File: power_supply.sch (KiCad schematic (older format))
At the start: 68 parts, among them J1 USB-MICRO, J2 USB, Q1 SI4174DY, Q2 SI4463CDY, Q3 SW, U1 LM3914, U10 LT1494, U2 TPD2E001DRL, U3 MIC2185, U4 TPS2511, U5 MCP73833, U6 TPD2E001DRL, U7 BATT, U8 MAX9938T, U9 FDC6392S

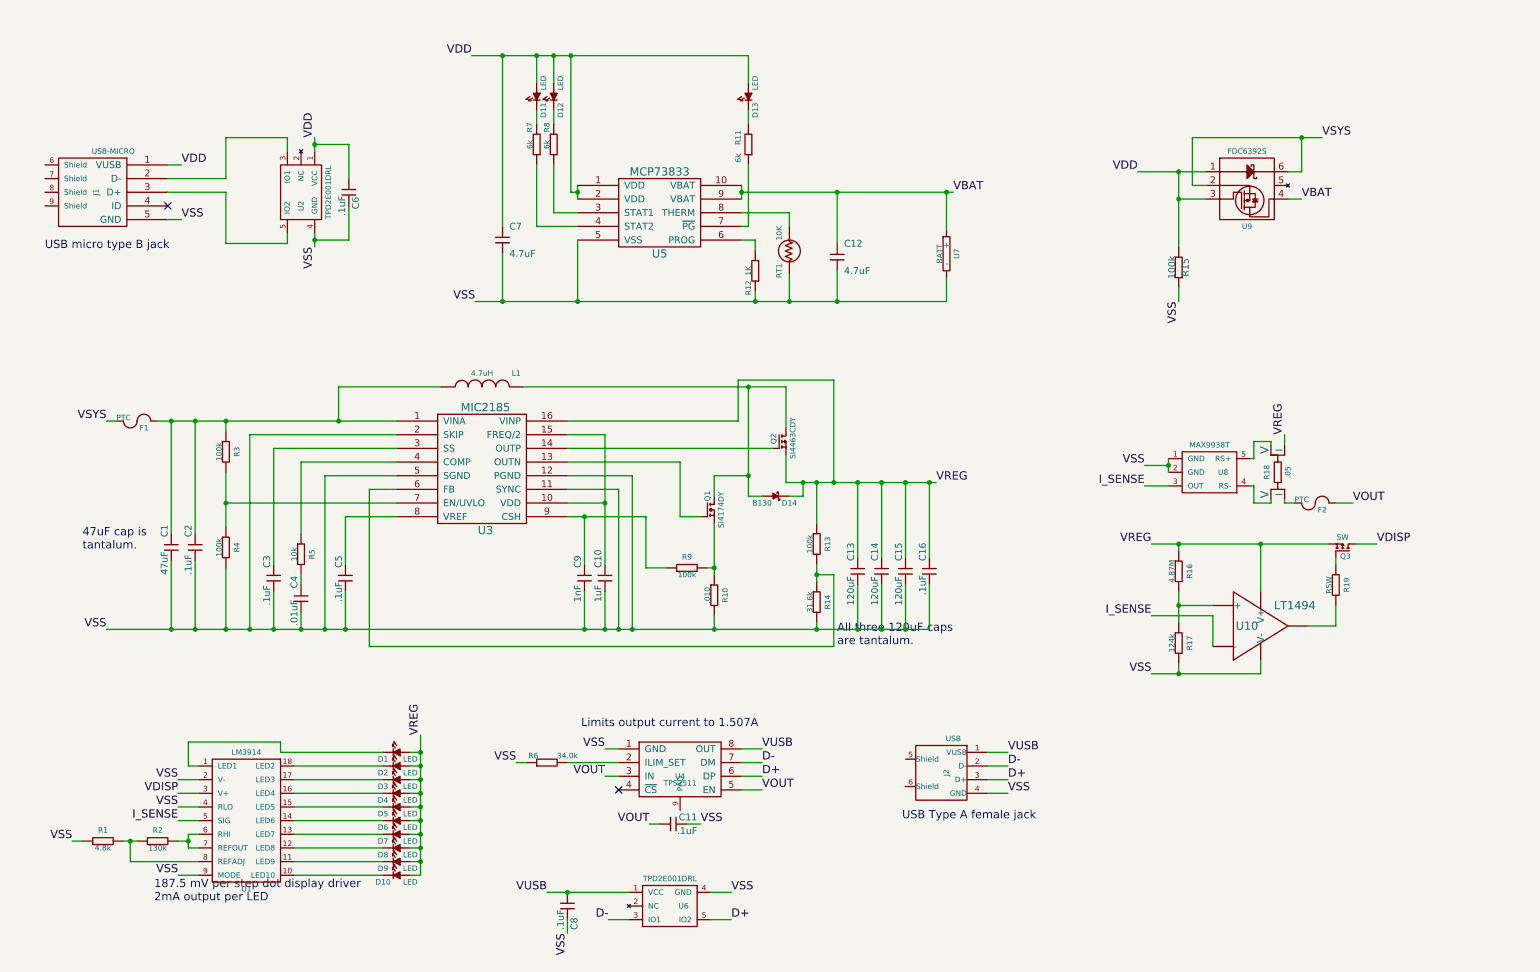
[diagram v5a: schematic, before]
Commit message: Updated comparator circuit to add histeresis.
Should turn on at .187V and off at .157V
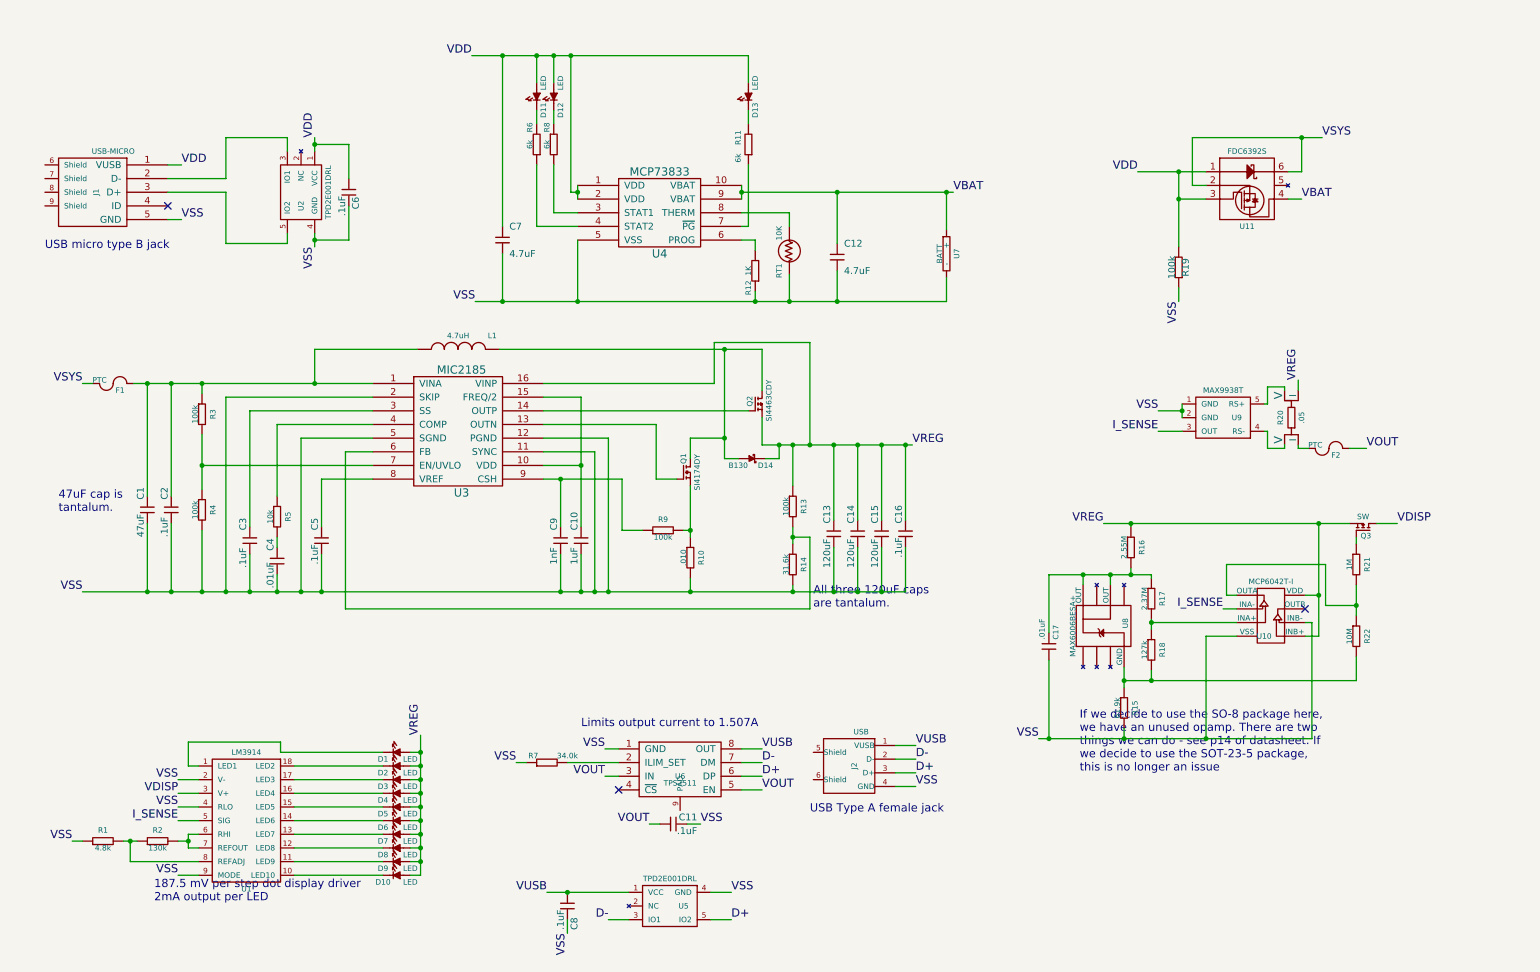
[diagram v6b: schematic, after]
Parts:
- removed U10: LT1494, symbol LT1494
- added C17: .01uF, symbol C
- added R15: 61.9k, ~, symbol R
- added R18: 127k, ~, symbol R
- added R22: 10M, ~, symbol R
- added U10: MCP6042T-I, symbol MCP6042
- added U8: MAX6006BESA+, symbol MAX6006
- R16: value 4.87M -> 2.55M
- R17: value 124k -> 2.37M
- R21: renamed from R19; value RSW -> 1M
- renumbered R15 to R19, R18 to R20, R7 to R6, R6 to R7, U9 to U11, U5 to U4, U6 to U5, U4 to U6, U8 to U9
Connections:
- net I_SENSE: now also U10.2 (INA-)
- net VREG: now also U10.5 (INB+), U10.8 (VDD)
- net VSS: now also C17.2, R15.2, U10.4 (VSS), U10.6 (INB-); no longer R17.2
- net at R16.2, R17.1: now also C17.1, U8.6 (OUT), U8.8 (OUT)
- net at R21.2: now also R22.1, U10.1 (OUTA)
- new net: R17.2, R18.1, U10.3 (INA+)
- new net: R15.1, R18.2, R22.2, U8.4 (GND)
- no-connect marks 2 -> 3
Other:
- note added: "If we decide to use the SO-8 package here, \nwe have an unused opamp. There are two \nthings we can do - see p14 of datasheet. If \nwe decide to use the SOT-23-5 package, \nthis is no longer an issue"
- moved on the sheet: C1, C10, C13, C14, C15, C16, C2, C3, C4, C5, C9, D14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

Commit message: Updated display auto-off circuit, added part numbers
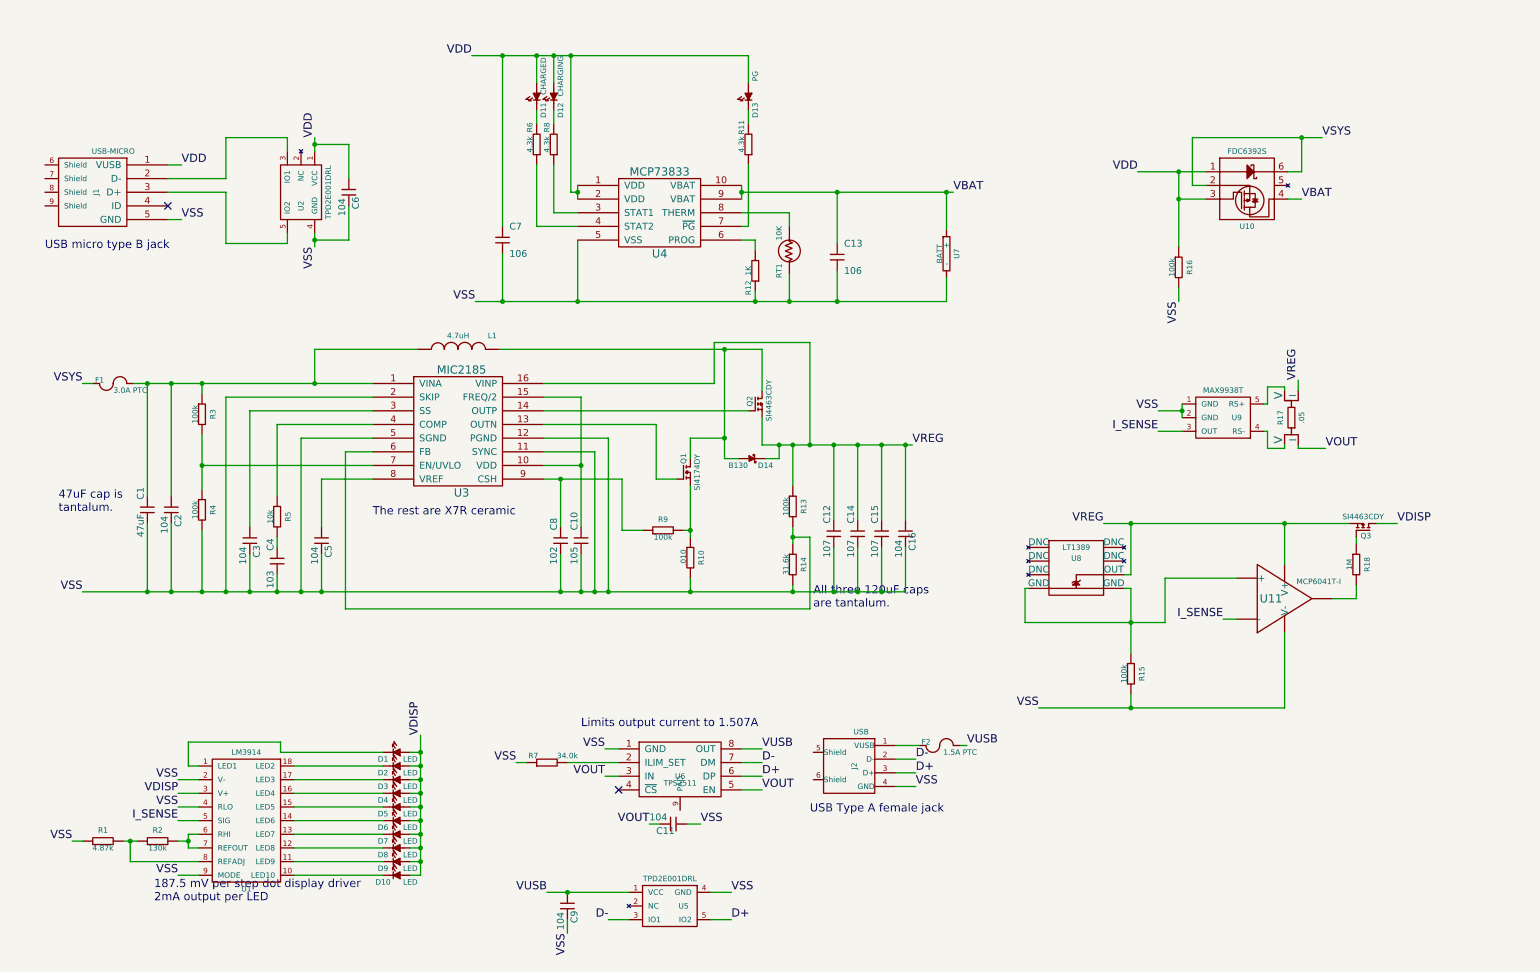
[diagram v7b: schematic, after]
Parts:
- removed C12: 4.7uF, symbol C
- removed C17: .01uF, symbol C
- removed C8: .1uF, symbol C
- removed R17: 2.37M, ~, symbol R
- removed R18: 127k, ~, symbol R
- removed R19: 100k, symbol R
- removed R22: 10M, ~, symbol R
- removed U10: MCP6042T-I, symbol MCP6042
- removed U8: MAX6006BESA+, symbol MAX6006
- added C13: 106, symbol C
- added C9: 104, symbol C
- added U11: MCP6041T-I, ~, symbol OPAMP
- added U8: LT1389, symbol LT1389
- C1: Product Number (none) -> 718-1362-1-ND; Vendor (none) -> Digikey
- C10: value 1uF -> 105; Product Number (none) -> 399-9714-ND; Vendor (none) -> Digikey
- C11, C16, C2, C3, C5, C6: value .1uF -> 104; Product Number (none) -> 399-1249-1-ND; Vendor (none) -> Digikey
- C12: renamed from C13; value 120uF -> 107; Product Number (none) -> 718-1885-1-ND; Vendor (none) -> Digikey
- C14, C15: value 120uF -> 107; Product Number (none) -> 718-1885-1-ND; Vendor (none) -> Digikey
- C4: value .01uF -> 103; Product Number (none) -> 399-9858-1-ND; Vendor (none) -> Digikey
- C7: value 4.7uF -> 106; Product Number (none) -> 399-7443-1-ND; Vendor (none) -> Digikey
- C8: renamed from C9; value 1nF -> 102; Product Number (none) -> 399-4144-ND; Vendor (none) -> Digikey
- D1, D2, D3, D4, D5, D6, D7: Product Number (none) -> 754-1439-1-ND; Vendor (none) -> Digikey
- D10: Product Number (none) -> 754-1143-1-ND; Vendor (none) -> Digikey
- D11: value LED -> CHARGED; Product Number (none) -> 754-1439-1-ND; Vendor (none) -> Digikey
- D12: value LED -> CHARGING; Product Number (none) -> 754-1136-1-ND; Vendor (none) -> Digikey
- D13: value LED -> PG; Product Number (none) -> 754-1439-1-ND; Vendor (none) -> Digikey
- D14: Digikey Product Number B130-E3/5ATGICT-ND -> (none); Product Number (none) -> B130-E3/5ATGICT-ND; Vendor (none) -> Digikey
- D8, D9: Product Number (none) -> 754-1140-1-ND; Vendor (none) -> Digikey
- F1: value PTC -> 3.0A PTC; Product Number (none) -> F4162CT-ND; Vendor (none) -> Digikey
- F2: value PTC -> 1.5A PTC; Product Number (none) -> F2154CT-ND; Vendor (none) -> Digikey
- J1: Digikey Product Number A108263CT-ND -> (none); Product Number (none) -> A108263CT-ND; Vendor (none) -> Digikey
- J2: Product Number (none) -> A31726-ND; Vendor (none) -> Digikey
- L1: Digikey Product Number SRR1240-4R7MCT-ND -> (none); Product Number (none) -> SRR1240-4R7MCT-ND; Vendor (none) -> Digikey
- Q1: Digikey Product Number SI4174DY-T1-GE3CT-ND -> (none); Product Number (none) -> SI4174DY-T1-GE3CT-ND; Vendor (none) -> Digikey
- Q2: Mouser Product Number 78-SI4463CDY-T1-GE3 -> (none); Product Number (none) -> 78-SI4463CDY-T1-GE3; Vendor (none) -> Mouser
- Q3: value SW -> SI4463CDY; Product Number (none) -> 78-SI4463CDY-T1-GE3; Vendor (none) -> Mouser
- R1: value 4.8k -> 4.87k; Product Number (none) -> CMF4.87KHFCT-ND; Vendor (none) -> Digikey
- R10: Product Number (none) -> LVRA-.01RCT-ND; Vendor (none) -> Digikey
- R11, R6, R8: value 6k -> 4.3k; Product Number (none) -> 4.3KH-ND; Vendor (none) -> Digikey
- R12: Product Number (none) -> 541-1.00KFCT-ND; Vendor (none) -> Digikey
- R13, R3, R4, R9: Product Number (none) -> 541-100KFCT-ND; Vendor (none) -> Digikey
- R14: Product Number (none) -> 541-31.6KFCT-ND; Vendor (none) -> Digikey
- R15: value 61.9k -> 100k; Product Number (none) -> 541-100KFCT-ND; Vendor (none) -> Digikey
- R16: value 2.55M -> 100k; Product Number (none) -> 541-100KFCT-ND; Vendor (none) -> Digikey
- R17: renamed from R20; Digikey Product Number LVK12R050DERCT-ND -> (none); Product Number (none) -> LVK12R050DERCT-ND; Vendor (none) -> Digikey
- R18: renamed from R21; Product Number (none) -> PPC1.00MXCT-ND; Vendor (none) -> Digikey
- R2: Product Number (none) -> CMF130KQFCT-ND; Vendor (none) -> Digikey
- R5: Product Number (none) -> PPC10.0KZCT-ND; Vendor (none) -> Digikey
- R7: Product Number (none) -> CMF34.0KHFCT-ND; Vendor (none) -> Digikey
- RT1: Product Number (none) -> BC2395CT-ND; Vendor (none) -> Digikey
- U1: Digikey Product Number LM3914N-1/NOPB-ND -> (none); Product Number (none) -> LM3914N-1/NOPB-ND; Vendor (none) -> Digikey
- U10: renamed from U11; Product Number (none) -> 512-FDC6392S; Vendor (none) -> Digikey
- U2, U5: Digikey Product Number 296-21883-1-ND -> (none); Product Number (none) -> 296-21883-1-ND; Vendor (none) -> Digikey
- U3: Product Number (none) -> 576-2162-ND; Vendor (none) -> Digikey
- U4: Product Number (none) -> MCP73833-FCI/UN-ND; Vendor (none) -> Digikey
- U6: Digikey Product Number 296-30552-1-ND -> (none); Product Number (none) -> 296-30552-1-ND; Vendor (none) -> Digikey
- U7: Product Number (none) -> 5702; Vendor (none) -> batteryspace
- U9: Digikey Product Number MAX9938TEUK+TCT-ND -> (none); Product Number (none) -> MAX9938TEUK+TCT-ND; Vendor (none) -> Digikey
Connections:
- net I_SENSE: now also U11.2 (-)
- net VBAT: now also C13.1
- net VDD: now also R16.1
- net VDISP: now also D1.1 (A), D10.1 (A), D2.1 (A), D3.1 (A), D4.1 (A), D5.1 (A), D6.1 (A), D7.1 (A), D8.1 (A), D9.1 (A)
- net VOUT: now also C11.2, R17.I2 (I); no longer C11.1, F2.2
- net VREG: now also U11.7 (V+), U8.6 (OUT); no longer D1.1 (A), D10.1 (A), D2.1 (A), D3.1 (A), D4.1 (A), D5.1 (A), D6.1 (A), D7.1 (A), D8.1 (A), D9.1 (A), R16.1
- net VSS: now also C11.1, R16.2, C13.2, C9.2, U11.4 (V-); no longer C11.2
- net VUSB: now also F2.2, C9.1; no longer J2.1 (VUSB)
- net at U4.3 (STAT1): now also R8.1; no longer R8.2
- net at D12.2 (K): now also R8.2; no longer R8.1
- net at F2.1: now also J2.1 (VUSB); no longer R17.I2 (I)
- net at R18.2: now also U11.6
- net at R15.1: now also U11.3 (+), U8.4 (GND), U8.5 (GND)
- no-connect marks 3 -> 2
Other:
- note added: "The rest are X7R ceramic"
- note removed: "If we decide to use the SO-8 package here, \nwe have an unused opamp. There are two \nthings we can do - see p14 of datasheet. If \nwe decide to use the SOT-23-5 package, \nthis is no longer an issue"
- moved on the sheet: F2

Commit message: Finished footprints. Began layout
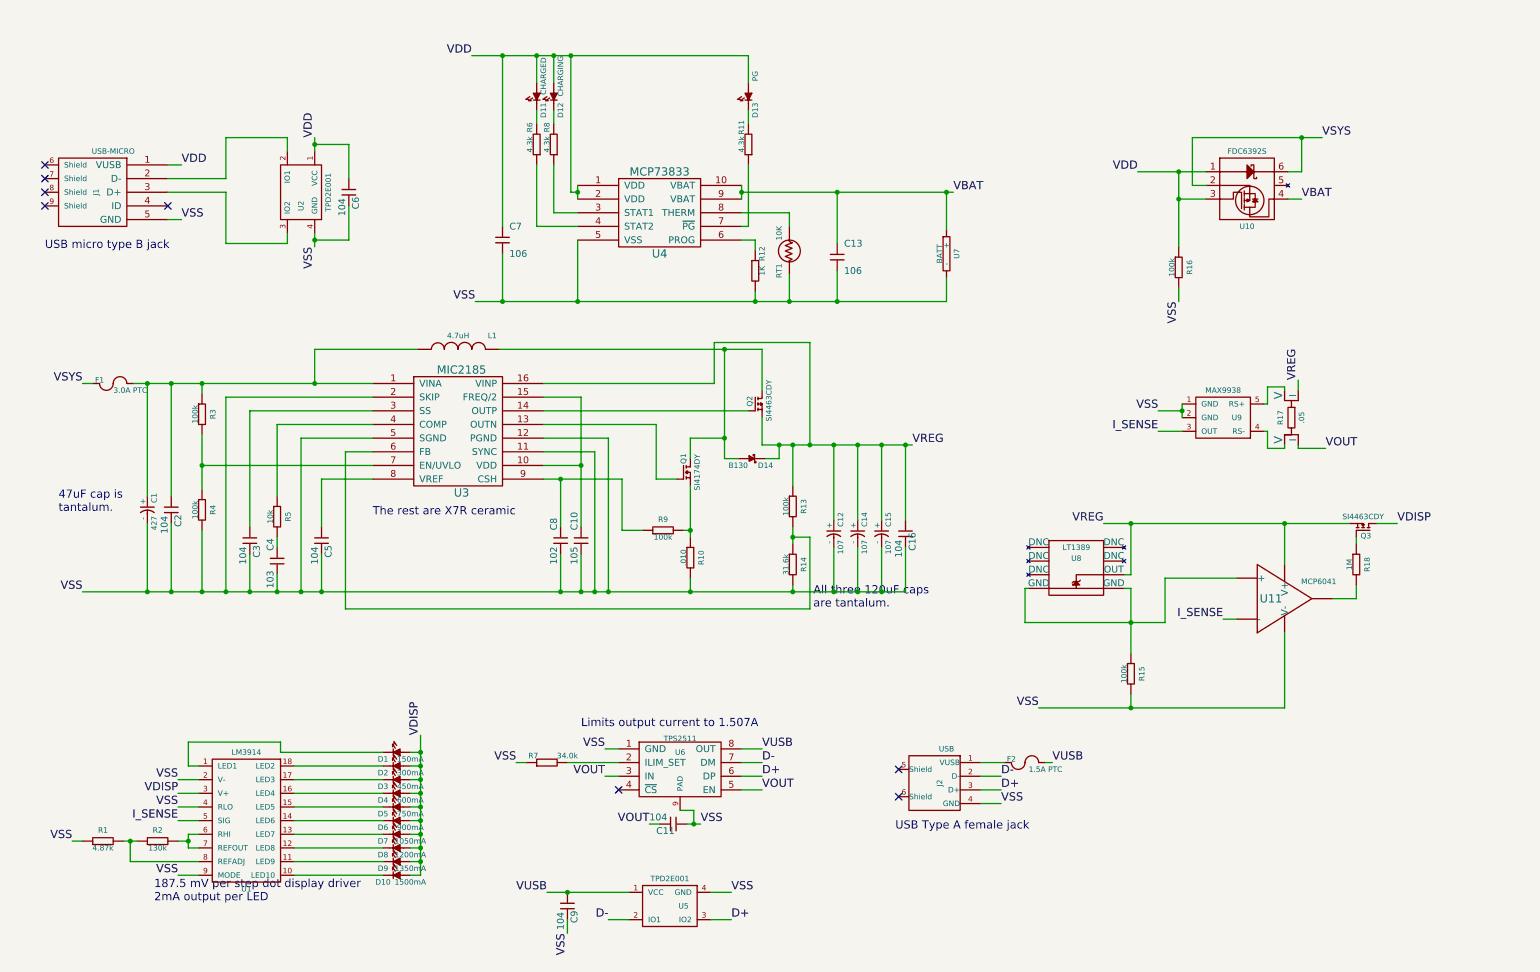
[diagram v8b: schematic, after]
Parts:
- removed C1: 47uF, symbol C
- removed C12, C14, C15: 107, symbol C
- removed U2, U5: TPD2E001DRL, symbol TPD2E001DRL
- added C1: 427, ~, symbol C_POL
- added C12, C14, C15: 107, ~, symbol C_POL
- added U2, U5: TPD2E001, ~, symbol TPD2E001DZD
- D1: value LED -> 150mA
- D10: value LED -> 1500mA
- D2: value LED -> 300mA
- D3: value LED -> 450mA
- D4: value LED -> 600mA
- D5: value LED -> 750mA
- D6: value LED -> 900mA
- D7: value LED -> 1050mA
- D8: value LED -> 1200mA
- D9: value LED -> 1350mA
- J2: Product Number A31726-ND -> A107360-ND
- R10: Product Number LVRA-.01RCT-ND -> WSLP-.01CT-ND
- R11, R6, R8: Product Number 4.3KH-ND -> 4.3KQBK-ND
- R18: Product Number PPC1.00MXCT-ND -> CMF1.00MHFCT-ND
- R2: Product Number CMF130KQFCT-ND -> CMF130KHFCT-ND
- RT1: Product Number BC2395CT-ND -> 541-1144-1-ND
- U10: Product Number 512-FDC6392S -> FDC6392SCT-ND
- U11: value MCP6041T-I -> MCP6041
- U9: value MAX9938T -> MAX9938
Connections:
- net D+: now also U5.3 (IO2)
- net D-: now also U5.2 (IO1)
- net VDD: now also U2.1 (VCC)
- net VOUT: now also R17.I1 (I); no longer R17.I2 (I)
- net VREG: now also R17.I2 (I), C12.1 (+), C14.1 (+), C15.1 (+); no longer R17.I1 (I)
- net VSS: now also R12.2, U6.9 (PAD), C1.2 (-), C12.2 (-), C14.2 (-), C15.2 (-), U2.4 (GND), U5.4 (GND); no longer R12.1
- net VUSB: now also U5.1 (VCC)
- net at J1.2 (D-): now also U2.2 (IO1)
- net at J1.3 (D+): now also U2.3 (IO2)
- net at C2.1, F1.2, L1.1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: now also C1.1 (+)
- net at U9.4 (RS-): now also R17.V1 (V); no longer R17.V2 (V)
- net at U9.5 (RS+): now also R17.V2 (V); no longer R17.V1 (V)
- net at U4.6 (PROG): now also R12.1; no longer R12.2
- no-connect marks 2 -> 8
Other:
- moved on the sheet: F2, J2
